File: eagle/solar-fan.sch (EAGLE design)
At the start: 44 parts, among them J1 POWER_JACKPTH, J3 7805, J6 USB_, U1 LT3652, U2 ATTINY85

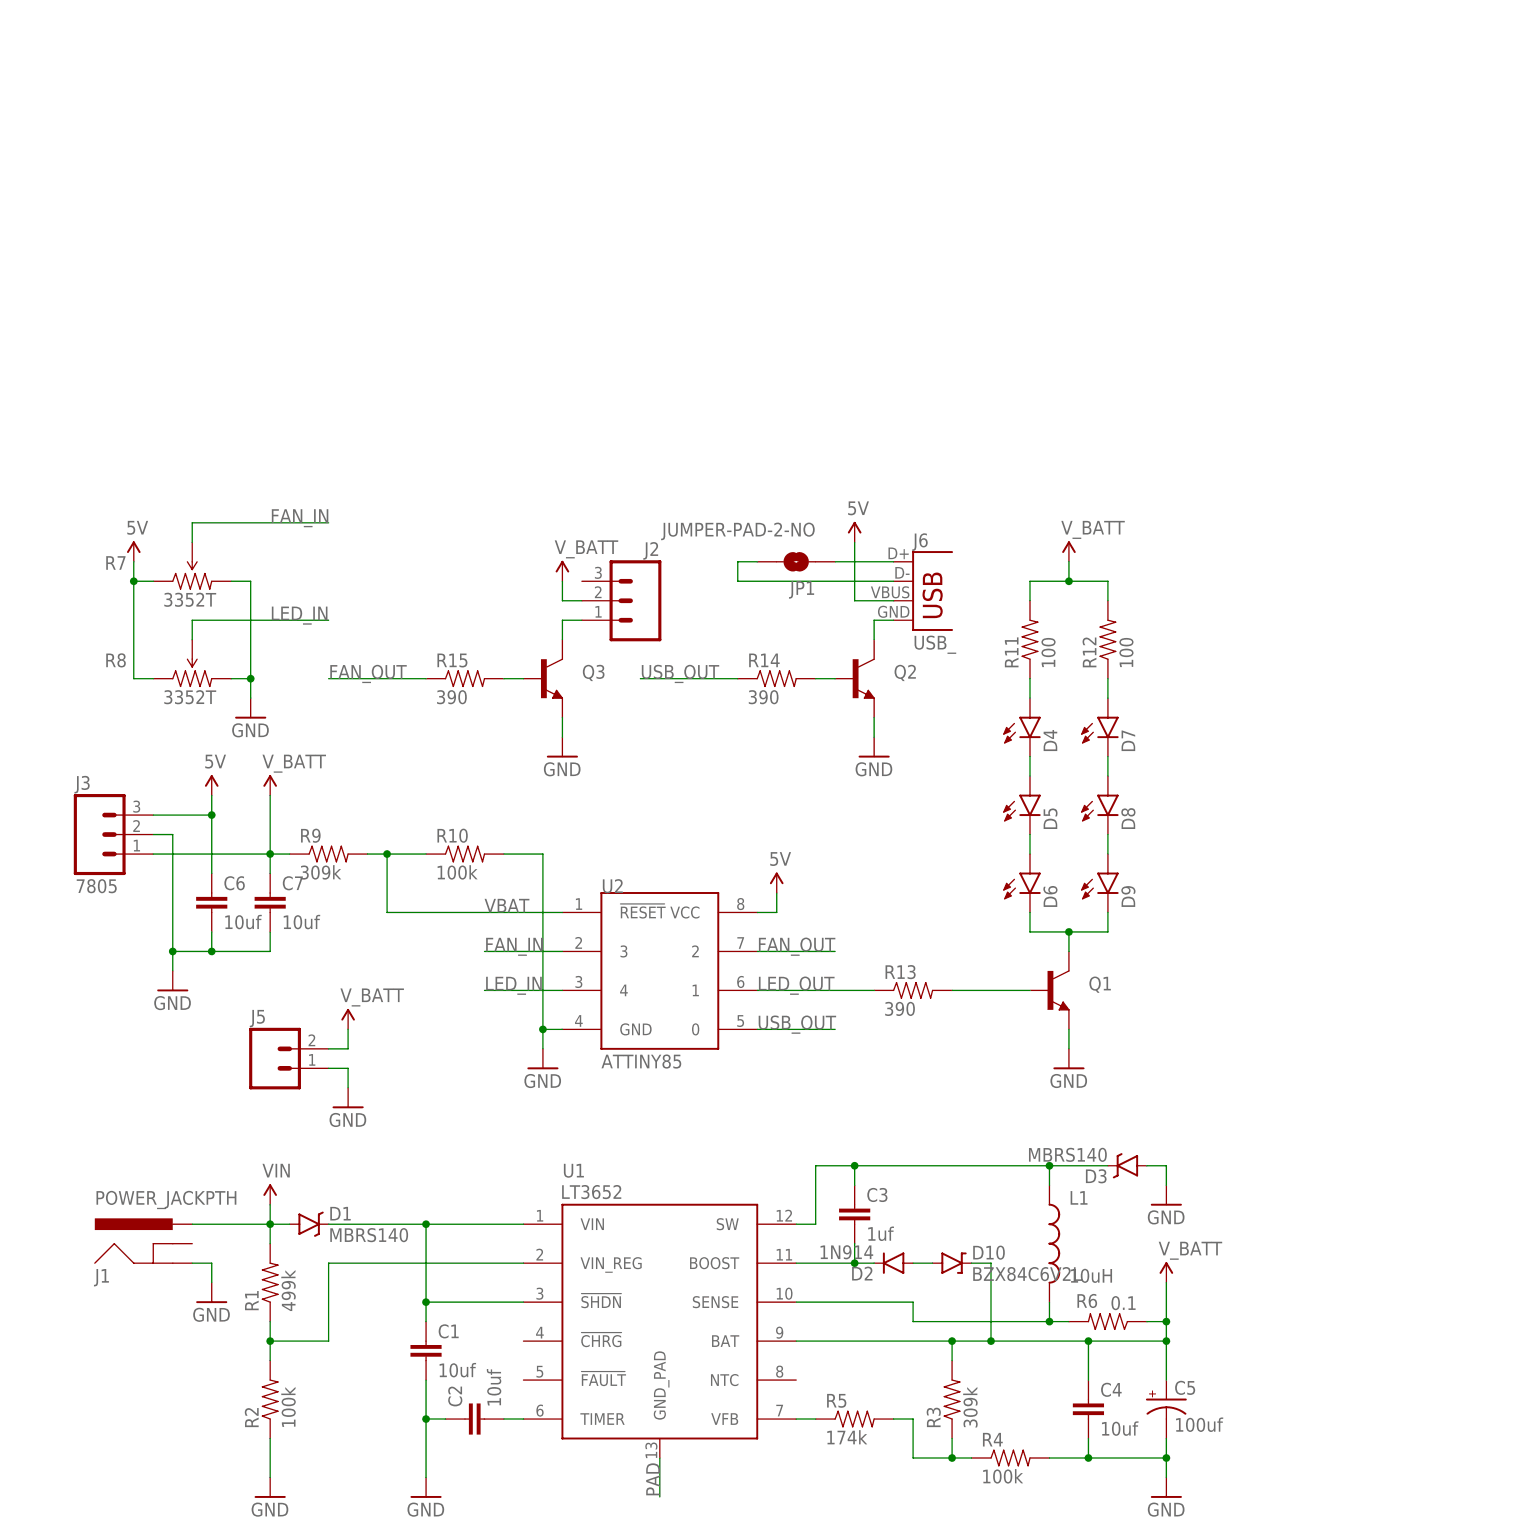
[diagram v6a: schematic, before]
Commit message: - updated charge voltage - led/cap placement - proper fan vs. usb out on micro - changed transistors to smd - solder mask change for gnd pad - added status leds for chager - changed battery/solar connectors
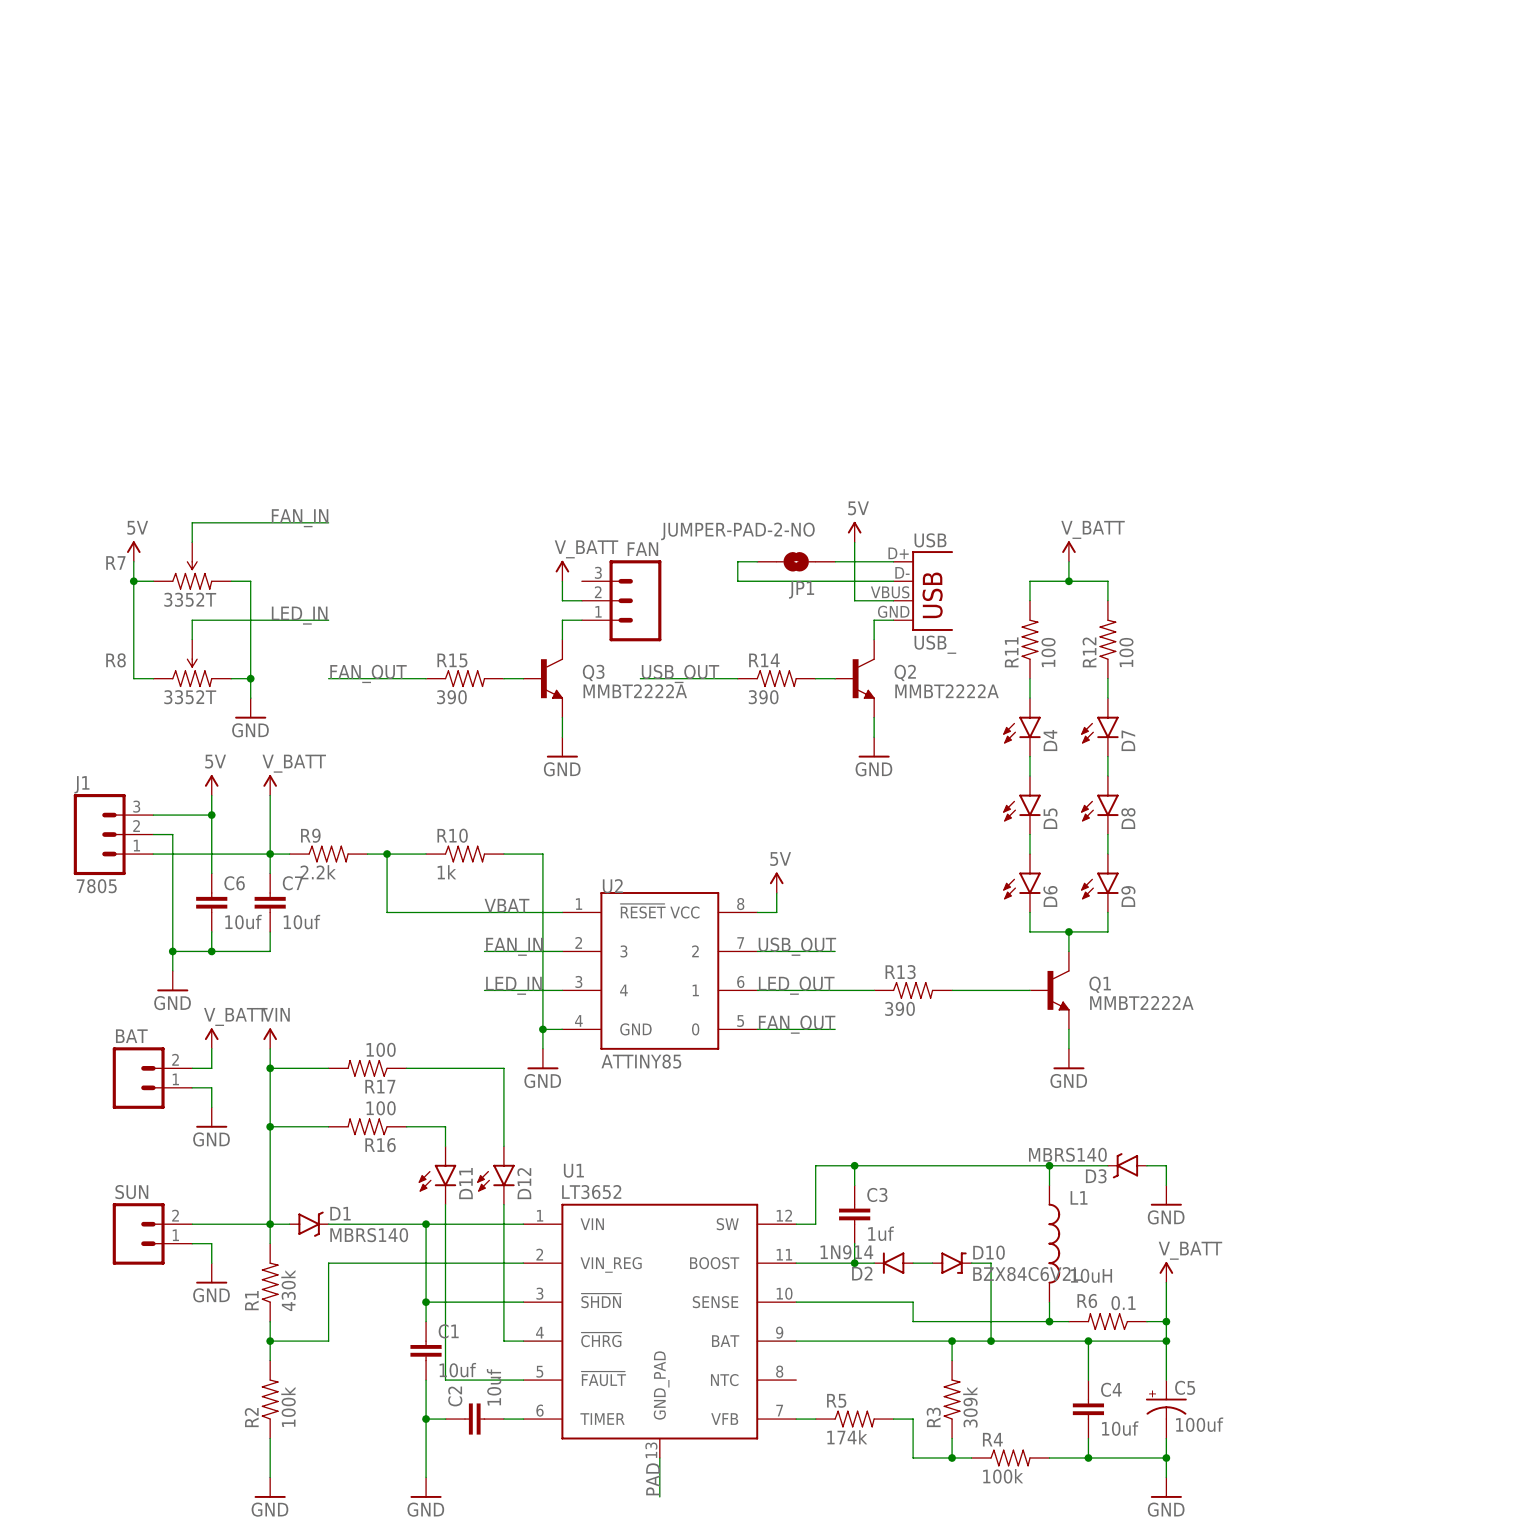
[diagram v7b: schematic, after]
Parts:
- removed J3: 7805, SparkFun-Connectors:M03PTH
- removed J5: (no value), SparkFun-Connectors:M02JST-PTH-2
- added BAT, SUN: (no value), SparkFun-Connectors:M025MM
- added D11, D12: (no value), SparkFun-LED:LED-WHITE0603
- added R16, R17: 100, SparkFun-Passives:RESISTOR0603-RES
- J1: value POWER_JACKPTH -> 7805; device SparkFun-Connectors:POWER_JACKPTH -> SparkFun-Connectors:M03PTH; PN CP-202A-ND -> 811-2196-5-ND; PN2 (none) -> 811-2196-5-ND
- Q1, Q2, Q3: value (none) -> MMBT2222A; device SparkFun-DiscreteSemi:TRANSISTOR_NPNP2N2222A -> SparkFun-DiscreteSemi:TRANSISTOR_NPNMMBT2222A; PN PN2222AFS-ND -> MMBT2222AFSCT-ND
- R1: value 499k -> 430k; PN P499KHCT-ND -> P430GCT-ND
- R10: value 100k -> 1k; PN P100KHCT-ND -> P1.00KHCT-ND
- R9: value 309k -> 2.2k; PN P309KHCT-ND -> P2.20KHCT-ND
- renumbered J2 to FAN, J6 to USB
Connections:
- new net N$11: D12.A, R17.1
- new net N$12: D12.C, U1.!CHRG
- new net N$20: D11.C, U1.!FAULT
- new net N$22: D11.A, R16.1
- net 5V: now also J1.3; no longer J3.3
- net FAN_OUT: now also U2.0; no longer U2.2
- net GND: now also BAT.1, J1.2, SUN.1; no longer J1.GND, J3.2, J5.1
- net USB_OUT: now also U2.2; no longer U2.0
- net VIN: now also R16.2, R17.2, SUN.2; no longer J1.PWR
- net V_BATT: now also BAT.2, J1.1; no longer J3.1, J5.2

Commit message: rev A build
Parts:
- added F1: PTC0603, SparkFun-PowerIC:PTC0603
- D11: PN 1516-1057-1-ND -> 160-1436-1-ND
- D12: PN 1516-1057-1-ND -> 160-1437-1-ND
- R1: PN P430GCT-ND -> P430KGCT-ND
- R16, R17: value 100 -> 10K; PN P100HCT-ND -> P10KGCT-ND
- renumbered J1 to +5V
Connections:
- new net N$23: BAT.2, F1.1
- net V_BATT: now also F1.2; no longer BAT.2
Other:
- moved on the sheet: BAT, C1, D11, D12
